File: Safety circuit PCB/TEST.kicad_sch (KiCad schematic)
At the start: 30 parts, among them J1 430450801, J2 430450801, Q1 2N7002K, Q2 2N7002K, Q3 2N7002K, Q4 2N7002K, Q5 2N7002K, Q6 2N7002K, Q7 2N7002K

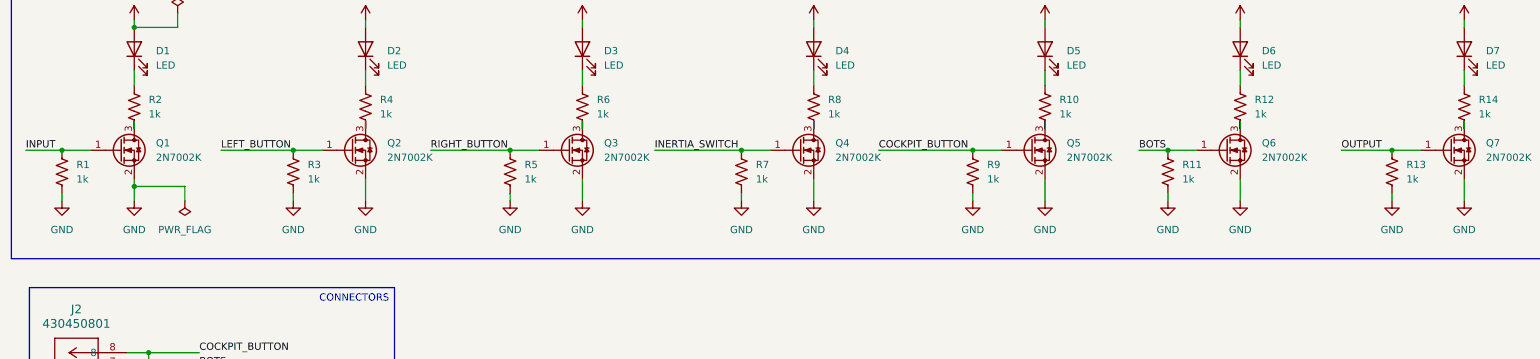
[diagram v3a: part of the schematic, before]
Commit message: Implement improvement advice from Jacob
Add ground vias next to all NMOS grounds

Change pull-down resistors at gates of NMOS to 100k from 1k, and change datasheet and resistor fields (part #, JLC Part #, etc...) accordingly

Make 12V power track 0.5 mm from 0.3mm

Add falstad simulation text file to Safety Circuit project

ERC and DRC still all pass
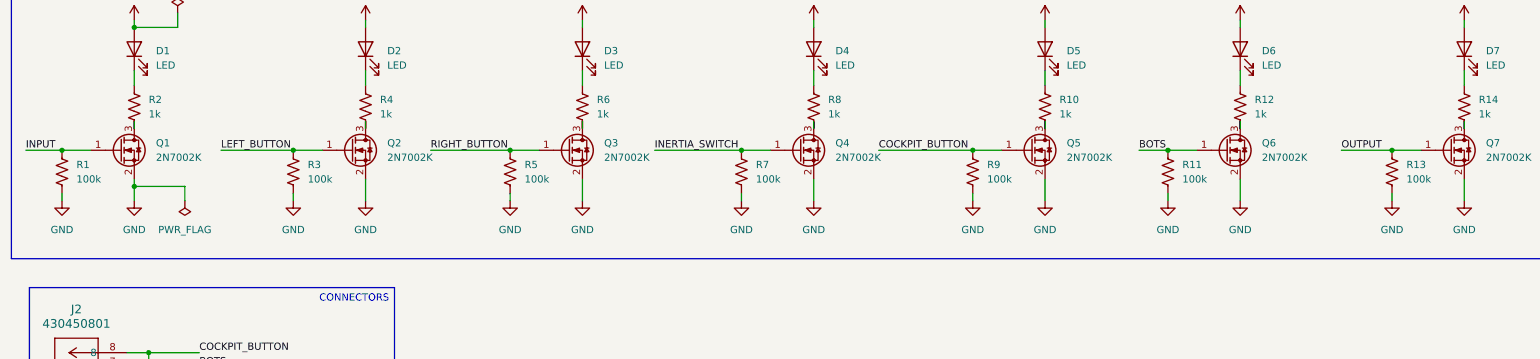
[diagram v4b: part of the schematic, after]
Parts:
- J1, J2: footprint CONN_SD-43045-001_08_MOL -> SC:CONN_SD-43045-001_08_MOL
- R1, R11, R13, R3, R5, R7, R9: value 1k -> 100k; Digikey https://www.digikey.com/en/products/detail/vishay-dale/CRCW08051K00FKEA/1175637 -> https://www.digikey.com/en/products/detail/vishay-dale/CRCW0805100KJNEA/1175246; MFR Part # CRCW08051K00FKEA -> CRCW0805100KJNEA
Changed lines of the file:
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@@
 			)
 		)
-		(property "Value" "1k"
+		(property "Value" "100k"
 			(at 257.81 48.2599 0)
 			(effects
@@
 			)
 		)
-		(property "Datasheet" "https://jlcpcb.com/api/file/downloadByFileSystemAccessId/8588950168741404672"
+		(property "Datasheet" "https://jlcpcb.com/api/file/downloadByFileSystemAccessId/8590171393792389120"
 			(at 255.27 46.99 0)
 			(effects
@@
 			)
 		)
-		(property "Digikey" "https://www.digikey.com/en/products/detail/vishay-dale/CRCW08051K00FKEA/1175637"
+		(property "Digikey" "https://www.digikey.com/en/products/detail/vishay-dale/CRCW0805100KJNEA/1175246"
 			(at 255.27 46.99 0)
 			(effects
@@
 			)
 		)
-		(property "MFR Part #" "CRCW08051K00FKEA"
+		(property "MFR Part #" "CRCW0805100KJNEA"
 			(at 255.27 46.99 0)
 			(effects
@@
 			)
 		)
-		(property "Footprint" "CONN_SD-43045-001_08_MOL"
+		(property "Footprint" "SC:CONN_SD-43045-001_08_MOL"
 			(at 33.274 105.156 0)
 			(effects
@@
 			)
 		)
-		(property "Value" "1k"
+		(property "Value" "100k"
 			(at 143.51 48.2599 0)
 			(effects
@@
 			)
 		)
-		(property "Datasheet" "https://jlcpcb.com/api/file/downloadByFileSystemAccessId/8588950168741404672"
+		(property "Datasheet" "https://jlcpcb.com/api/file/downloadByFileSystemAccessId/8590171393792389120"
 			(at 140.97 46.99 0)
 			(effects
@@
 			)
 		)
-		(property "Digikey" "https://www.digikey.com/en/products/detail/vishay-dale/CRCW08051K00FKEA/1175637"
+		(property "Digikey" "https://www.digikey.com/en/products/detail/vishay-dale/CRCW0805100KJNEA/1175246"
 			(at 140.97 46.99 0)
 			(effects
@@
 			)
 		)
-		(property "MFR Part #" "CRCW08051K00FKEA"
+		(property "MFR Part #" "CRCW0805100KJNEA"
 			(at 140.97 46.99 0)
 			(effects
@@
 			)
 		)
-		(property "Value" "1k"
+		(property "Value" "100k"
 			(at 218.44 48.2599 0)
 			(effects
@@
 			)
 		)
-		(property "Datasheet" "https://jlcpcb.com/api/file/downloadByFileSystemAccessId/8588950168741404672"
+		(property "Datasheet" "https://jlcpcb.com/api/file/downloadByFileSystemAccessId/8590171393792389120"
 			(at 215.9 46.99 0)
 			(effects
@@
 			)
 		)
-		(property "Digikey" "https://www.digikey.com/en/products/detail/vishay-dale/CRCW08051K00FKEA/1175637"
+		(property "Digikey" "https://www.digikey.com/en/products/detail/vishay-dale/CRCW0805100KJNEA/1175246"
 			(at 215.9 46.99 0)
 			(effects
@@
 			)
 		)
-		(property "MFR Part #" "CRCW08051K00FKEA"
+		(property "MFR Part #" "CRCW0805100KJNEA"
 			(at 215.9 46.99 0)
 			(effects
@@
 			)
 		)
-		(property "Value" "1k"
+		(property "Value" "100k"
 			(at 64.77 48.2599 0)
 			(effects
@@
 			)
 		)
-		(property "Datasheet" "https://jlcpcb.com/api/file/downloadByFileSystemAccessId/8588950168741404672"
+		(property "Datasheet" "https://jlcpcb.com/api/file/downloadByFileSystemAccessId/8590171393792389120"
 			(at 62.23 46.99 0)
 			(effects
@@
 			)
 		)
-		(property "Digikey" "https://www.digikey.com/en/products/detail/vishay-dale/CRCW08051K00FKEA/1175637"
+		(property "Digikey" "https://www.digikey.com/en/products/detail/vishay-dale/CRCW0805100KJNEA/1175246"
 			(at 62.23 46.99 0)
 			(effects
@@
 			)
 		)
-		(property "MFR Part #" "CRCW08051K00FKEA"
+		(property "MFR Part #" "CRCW0805100KJNEA"
 			(at 62.23 46.99 0)
 			(effects
@@
 			)
 		)
-		(property "Value" "1k"
+		(property "Value" "100k"
 			(at 24.13 48.2599 0)
 			(effects
@@
 			)
 		)
-		(property "Datasheet" "https://jlcpcb.com/api/file/downloadByFileSystemAccessId/8588950168741404672"
+		(property "Datasheet" "https://jlcpcb.com/api/file/downloadByFileSystemAccessId/8590171393792389120"
 			(at 21.59 46.99 0)
 			(effects
@@
 			)
 		)
-		(property "Digikey" "https://www.digikey.com/en/products/detail/vishay-dale/CRCW08051K00FKEA/1175637"
+		(property "Digikey" "https://www.digikey.com/en/products/detail/vishay-dale/CRCW0805100KJNEA/1175246"
 			(at 21.59 46.99 0)
 			(effects
@@
 			)
 		)
-		(property "MFR Part #" "CRCW08051K00FKEA"
+		(property "MFR Part #" "CRCW0805100KJNEA"
 			(at 21.59 46.99 0)
 			(effects
@@
 			)
 		)
-		(property "Footprint" "CONN_SD-43045-001_08_MOL"
+		(property "Footprint" "SC:CONN_SD-43045-001_08_MOL"
 			(at 33.274 139.446 0)
 			(effects
@@
 			)
 		)
-		(property "Value" "1k"
+		(property "Value" "100k"
 			(at 184.15 48.2599 0)
 			(effects
@@
 			)
 		)
-		(property "Datasheet" "https://jlcpcb.com/api/file/downloadByFileSystemAccessId/8588950168741404672"
+		(property "Datasheet" "https://jlcpcb.com/api/file/downloadByFileSystemAccessId/8590171393792389120"
 			(at 181.61 46.99 0)
 			(effects
@@
 			)
 		)
-		(property "Digikey" "https://www.digikey.com/en/products/detail/vishay-dale/CRCW08051K00FKEA/1175637"
+		(property "Digikey" "https://www.digikey.com/en/products/detail/vishay-dale/CRCW0805100KJNEA/1175246"
 			(at 181.61 46.99 0)
 			(effects
@@
 			)
 		)
-		(property "MFR Part #" "CRCW08051K00FKEA"
+		(property "MFR Part #" "CRCW0805100KJNEA"
 			(at 181.61 46.99 0)
 			(effects
@@
 			)
 		)
-		(property "Value" "1k"
+		(property "Value" "100k"
 			(at 102.87 48.2599 0)
 			(effects
@@
 			)
 		)
-		(property "Datasheet" "https://jlcpcb.com/api/file/downloadByFileSystemAccessId/8588950168741404672"
+		(property "Datasheet" "https://jlcpcb.com/api/file/downloadByFileSystemAccessId/8590171393792389120"
 			(at 100.33 46.99 0)
 			(effects
@@
 			)
 		)
-		(property "Digikey" "https://www.digikey.com/en/products/detail/vishay-dale/CRCW08051K00FKEA/1175637"
+		(property "Digikey" "https://www.digikey.com/en/products/detail/vishay-dale/CRCW0805100KJNEA/1175246"
 			(at 100.33 46.99 0)
 			(effects
@@
 			)
 		)
-		(property "MFR Part #" "CRCW08051K00FKEA"
+		(property "MFR Part #" "CRCW0805100KJNEA"
 			(at 100.33 46.99 0)
 			(effects

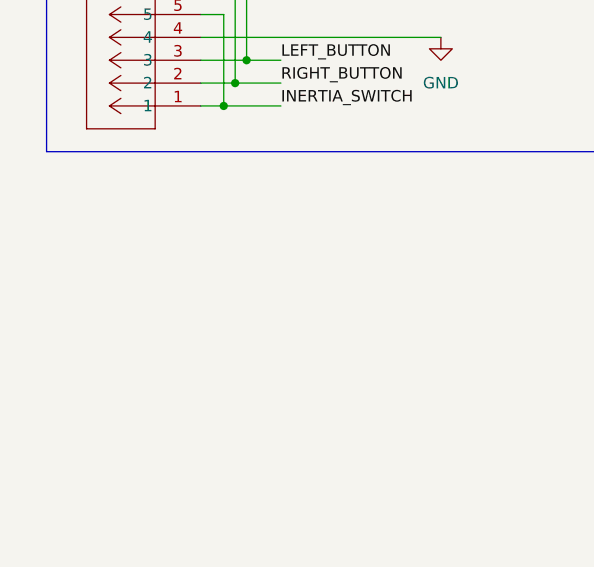
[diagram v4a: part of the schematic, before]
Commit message: Add Sammy connector footprint to Safety Circuit PCB
The PCB layout still needs to be redone once again to actually fit the connector. It seems like it will have to be extended around 0.8 inches. at a minimum.
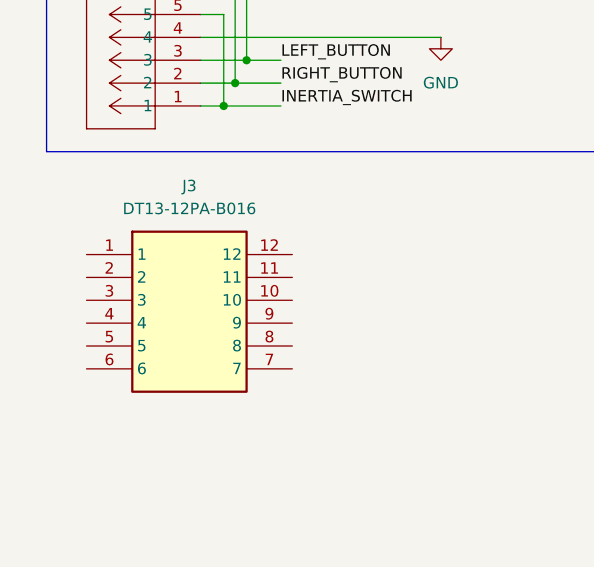
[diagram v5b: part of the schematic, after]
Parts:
- added J3: DT13-12PA-B016, DT1312PAB016, symbol TEConn:DT13-12PA-B016
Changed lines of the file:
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@@
+	)
+	(symbol
+		(lib_id "TEConn:DT13-12PA-B016")
+		(at 20.32 147.32 0)
+		(unit 1)
+		(exclude_from_sim no)
+		(in_bom yes)
+		(on_board yes)
+		(dnp no)
+		(fields_autoplaced yes)
+		(property "Reference" "J3"
+			(at 31.75 139.7 0)
+			(effects
+				(font
+					(size 1.27 1.27)
+				)
+			)
+		)
+		(property "Value" "DT13-12PA-B016"
+			(at 31.75 142.24 0)
+			(effects
+				(font
+					(size 1.27 1.27)
+				)
+			)
+		)
+		(property "Footprint" "DT1312PAB016"
+			(at 39.37 242.24 0)
+			(effects
+				(font
+					(size 1.27 1.27)
+				)
+				(justify left top)
+				(hide yes)
+			)
+		)
+		(property "Datasheet" "https://www.te.com/commerce/DocumentDelivery/DDEController?Action=srchrtrv&DocNm=1-1773962-8&DocType=Data%20Sheet&DocLang=English&PartCntxt=DT13-12PA-B016&DocFormat=pdf"
+			(at 39.37 342.24 0)
+			(effects
+				(font
+					(size 1.27 1.27)
+				)
+				(justify left top)
+				(hide yes)
+			)
+		)
+		(property "Description" "Body Features: Primary Product Color Gray | Connector & Keying Code A | Configuration Features: Number of Rows 2 | Number of Positions 12 | PCB Mount Orientation Right Angle | Number of Sections 1 | Number of Signal Positions 12 | Contact Features: Contact Mating Area Plating Material Nickel | Contact Type Pin | Mating Pin Diameter 1.59 MM | Contact Current Rating (Max) 13 AMP | Mating Pin Diameter .063 INCH | Contact Size Size 16 | Dimensions: Profile Height from PCB 35.26 MM | PCB Thickness (Recommended)"
+			(at 20.32 147.32 0)
+			(effects
+				(font
+					(size 1.27 1.27)
+				)
+				(hide yes)
+			)
+		)
+		(property "Height" "35.26"
+			(at 39.37 542.24 0)
+			(effects
+				(font
+					(size 1.27 1.27)
+				)
+				(justify left top)
+				(hide yes)
+			)
+		)
+		(property "Mouser Part Number" "571-DT13-12PA-B016"
+			(at 39.37 642.24 0)
+			(effects
+				(font
+					(size 1.27 1.27)
+				)
+				(justify left top)
+				(hide yes)
+			)
+		)
+		(property "Mouser Price/Stock" "https://www.mouser.co.uk/ProductDetail/TE-Connectivity-DEUTSCH/DT13-12PA-B016?qs=vkMqrgFpRaiA6MCeYpv2Ag%3D%3D"
+			(at 39.37 742.24 0)
+			(effects
+				(font
+					(size 1.27 1.27)
+				)
+				(justify left top)
+				(hide yes)
+			)
+		)
+		(property "Manufacturer_Name" "TE Connectivity"
+			(at 39.37 842.24 0)
+			(effects
+				(font
+					(size 1.27 1.27)
+				)
+				(justify left top)
+				(hide yes)
+			)
+		)
+		(property "Manufacturer_Part_Number" "DT13-12PA-B016"
+			(at 39.37 942.24 0)
+			(effects
+				(font
+					(size 1.27 1.27)
+				)
+				(justify left top)
+				(hide yes)
+			)
+		)
+		(pin "9"
+		)
+		(pin "11"
+		)
+		(pin "10"
+		)
+		(pin "2"
+		)
+		(pin "6"
+		)
+		(pin "12"
+		)
+		(pin "4"
+		)
+		(pin "1"
+		)
+		(pin "3"
+		)
+		(pin "5"
+		)
+		(pin "7"
+		)
+		(pin "8"
+		)
+		(instances
+			(project ""
+				(path "/49768109-2e19-4295-adfa-599621ab46ec"
+					(reference "J3")
+					(unit 1)
+				)
+			)
+		)
 	)
 	(symbol

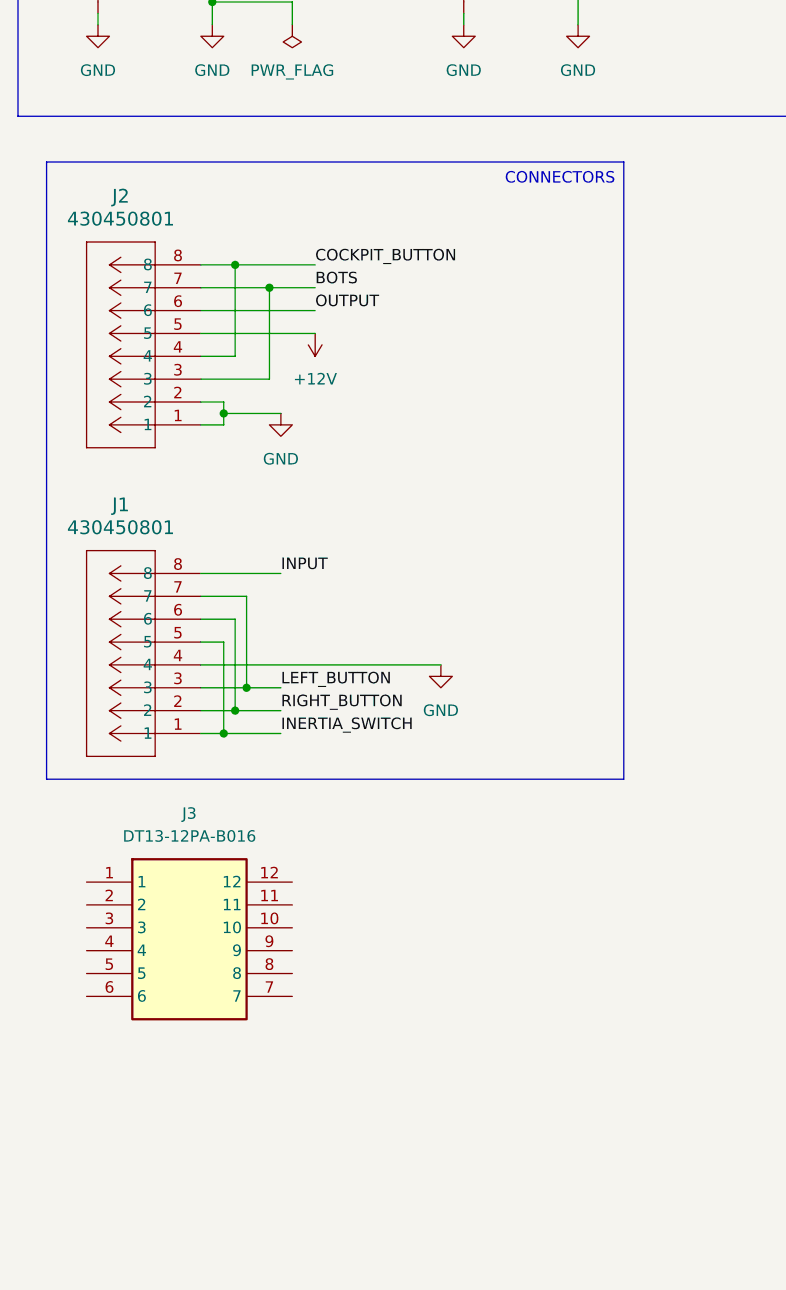
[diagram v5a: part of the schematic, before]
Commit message: Safety Circuit - Add Sammy Connector, Generate BOM, Generate Gerber and Drill Files
Safety circuit is about half an inch wider and half and inch less tall now
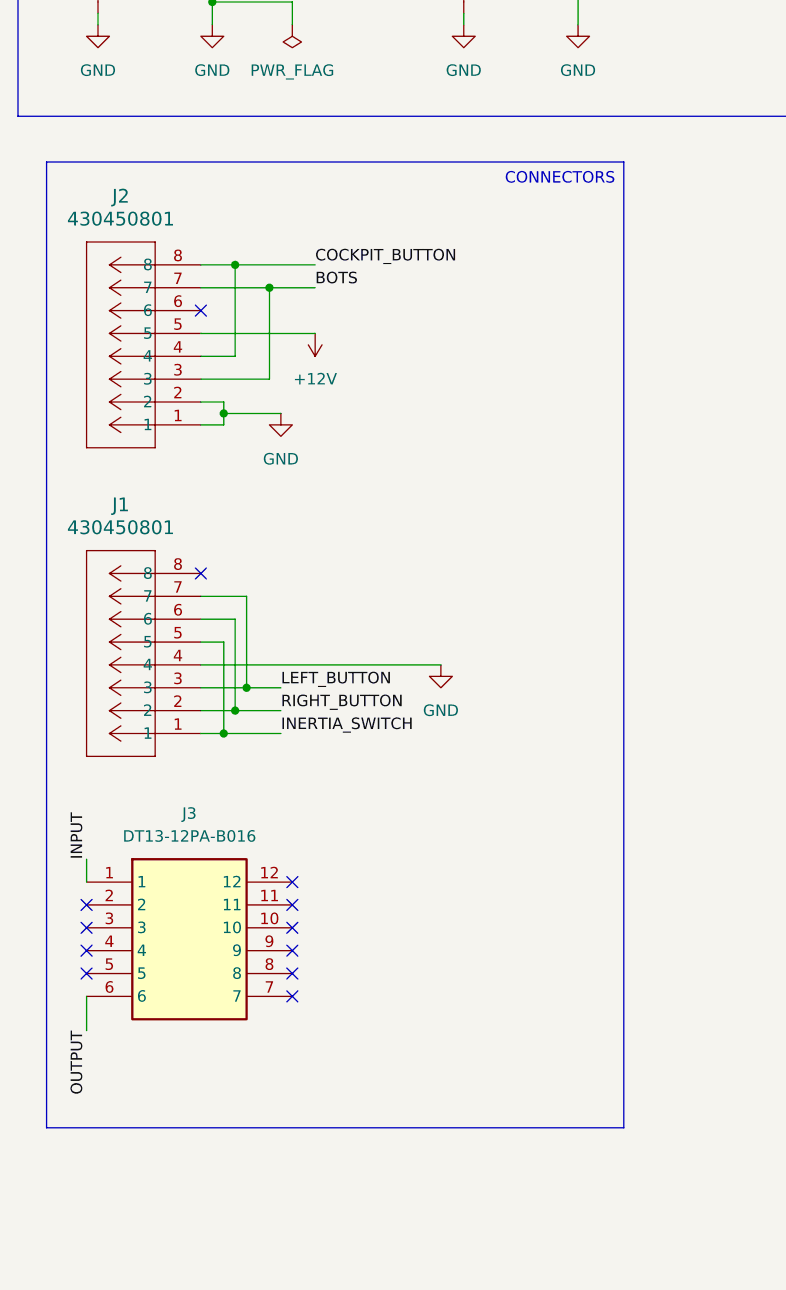
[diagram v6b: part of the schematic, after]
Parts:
- D1, D2, D3, D4, D5, D6, D7: JCL Datasheet https://jlcpcb.com/api/file/downloadByFileSystemAccessId/85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 -> (none); JCL Link https://jlcpcb.com/partdetail/23857065-PSC_1608U50GCG4/C223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 -> (none); JCL# C22371297 -> (none); JLC Datasheet (none) -> https://jlcpcb.com/api/file/downloadByFileSystemAccessId/85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; JLC Link (none) -> https://jlcpcb.com/partdetail/23857065-PSC_1608U50GCG4/C223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; JLC Part # (none) -> C22371297
- J1, J2: JCL Datasheet https://www.molex.com/content/dam/molex/molex-dot-com/produ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 -> (none); JCL Link https://jlcpcb.com/partdetail/MOLEX-430450801/C5765943 -> (none); JCL# C5765943 -> (none); JLC Datasheet (none) -> https://www.molex.com/content/dam/molex/molex-dot-com/produ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; JLC Link (none) -> https://jlcpcb.com/partdetail/MOLEX-430450801/C5765943; JLC Part # (none) -> C5765943
- J3: footprint DT1312PAB016 -> SC:DT1312PAB016; Drawing (none) -> https://www.te.com/commerce/DocumentDelivery/DDEController?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; JLC Datasheet (none) -> https://jlcpcb.com/api/file/downloadByFileSystemAccessId/86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; JLC Link (none) -> https://jlcpcb.com/partdetail/TEConnectivity-DT13_12PAB016/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; JLC Part # (none) -> C17266705; MFR Part # (none) -> DT13-12PA-B016; Manufacturer (none) -> TE Connectivity; Manufacturer_Name TE Connectivity -> (none); Manufacturer_Part_Number DT13-12PA-B016 -> (none); Mouser Part Number 571-DT13-12PA-B016 -> (none); Mouser Price/Stock https://www.mouser.co.uk/ProductDetail/TE-Connectivity-DEUT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 -> (none)
- Q1, Q2, Q3, Q4, Q5, Q6, Q7: JCL Datasheet https://jlcpcb.com/api/file/downloadByFileSystemAccessId/85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 -> (none); JCL Link https://jlcpcb.com/partdetail/VishayIntertech-2N7002K_T1GE3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 -> (none); JCL# C81445 -> (none); JLC Datasheet (none) -> https://jlcpcb.com/api/file/downloadByFileSystemAccessId/85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; JLC Link (none) -> https://jlcpcb.com/partdetail/VishayIntertech-2N7002K_T1GE3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; JLC Part # (none) -> C81445
- R1, R10, R11, R12, R13, R14, R2, R3, R4, R5, R6, R7, R8, R9: JCL Datasheet https://jlcpcb.com/api/file/downloadByFileSystemAccessId/85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 -> (none); JCL Link https://jlcpcb.com/partdetail/VishayIntertech-CRCW08051K00F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 -> (none); JCL# C844939 -> (none); JLC Datasheet (none) -> https://jlcpcb.com/api/file/downloadByFileSystemAccessId/85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; JLC Link (none) -> https://jlcpcb.com/partdetail/VishayIntertech-CRCW08051K00F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; JLC Part # (none) -> C844939
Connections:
- net INPUT: now also J3.1; no longer J1.8
- net OUTPUT: now also J3.6; no longer J2.6
- no-connect marks 0 -> 12
